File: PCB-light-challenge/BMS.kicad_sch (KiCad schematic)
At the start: 5 parts, among them U2 AP9101CK, U3 SP8K32FRATB

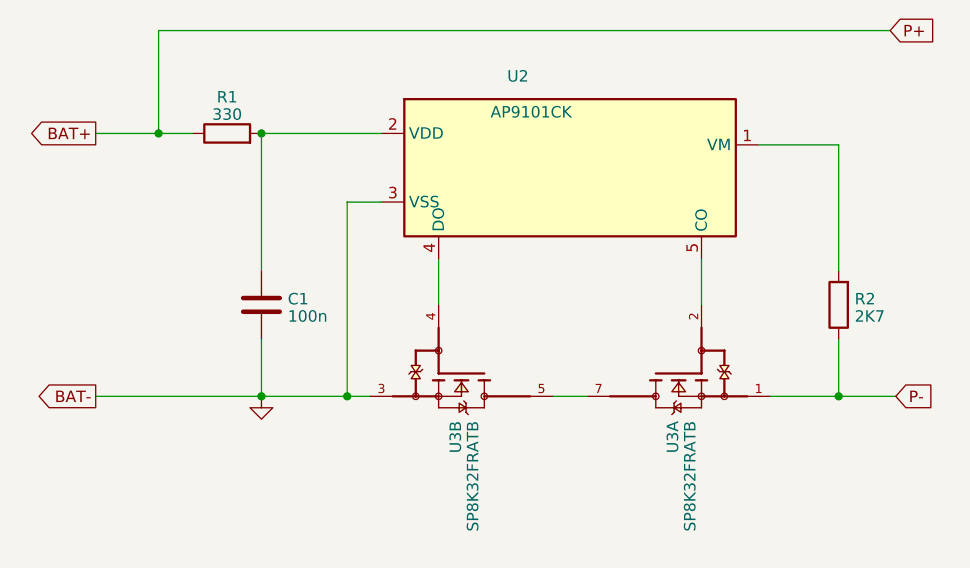
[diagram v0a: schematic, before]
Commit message: main board aangepast en ground toegevoegd
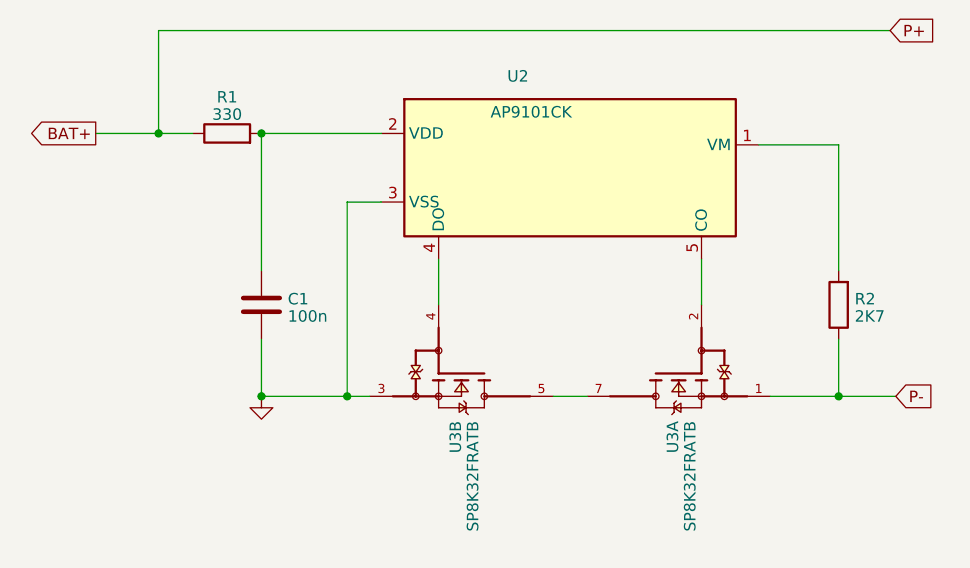
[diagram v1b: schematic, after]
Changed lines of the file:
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@@
-    (stroke (width 0) (type default))
-  )
-  (wire (pts (xy 55.88 74.295) (xy 74.295 74.295))
     (stroke (width 0) (type default))
   )
@@
     (stroke (width 0) (type default))
   )
-  (global_label "BAT-" (shape output) (at 55.88 74.295 180) (fields_autoplaced)
-    (effects (font (size 1.27 1.27)) (justify right))
-    (property "Intersheetrefs" "${INTERSHEET_REFS}" (at 48.0756 74.295 0)
-      (effects (font (size 1.27 1.27)) (justify right) hide)
-    )
-  )
   (global_label "P+" (shape input) (at 144.145 33.655 0) (fields_autoplaced)

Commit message: PCB 80% af
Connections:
- net P- is gone; now on net GND: R2.1, U3.1
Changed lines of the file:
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@@
     )
   )
-  (global_label "P-" (shape input) (at 144.78 74.295 0) (fields_autoplaced)
-    (effects (font (size 1.27 1.27)) (justify left))
-    (property "Intersheetrefs" "${INTERSHEET_REFS}" (at 150.5282 74.295 0)
-      (effects (font (size 1.27 1.27)) (justify left) hide)
+  (symbol (lib_id "power:GND") (at 144.78 74.295 0) (unit 1)
+    (in_bom yes) (on_board yes) (dnp no) (fields_autoplaced)
+    (property "Reference" "#PWR020" (at 144.78 80.645 0)
+      (effects (font (size 1.27 1.27)) hide)
+    )
+    (property "Value" "GND" (at 144.78 78.4305 0)
+      (effects (font (size 1.27 1.27)) hide)
+    )
+    (property "Footprint" "" (at 144.78 74.295 0)
+      (effects (font (size 1.27 1.27)) hide)
+    )
+    (property "Datasheet" "" (at 144.78 74.295 0)
+      (effects (font (size 1.27 1.27)) hide)
+    )
+    (pin "1")
+    (instances
+      (project "PCB-light-challenge"
+        (path "/35573e8f-7834-430c-81d2-239f316c7834/91ce53e5-ea08-4091-9289-d2f38a19ddbc"
+          (reference "#PWR020") (unit 1)
+        )
+      )
     )
   )
